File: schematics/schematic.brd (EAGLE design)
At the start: 180.3 x 63.5 mm, 22 parts, among them U1 TSR_1-2450

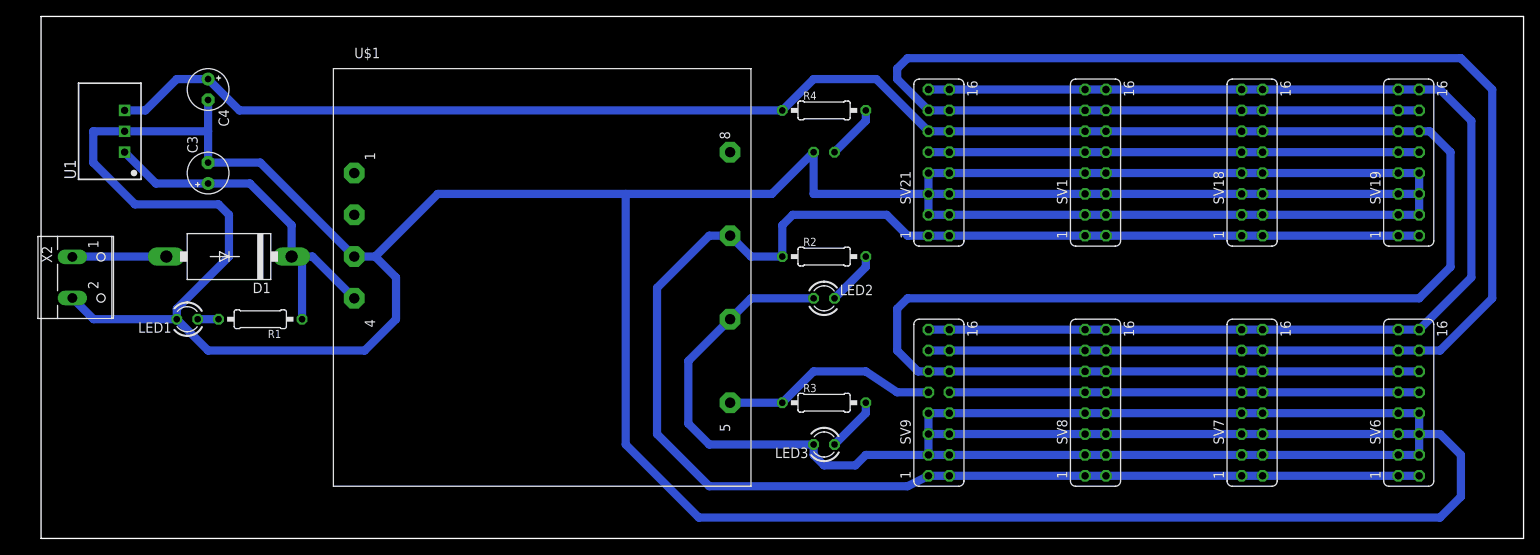
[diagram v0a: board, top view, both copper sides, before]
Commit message: added drillholes and descriptions
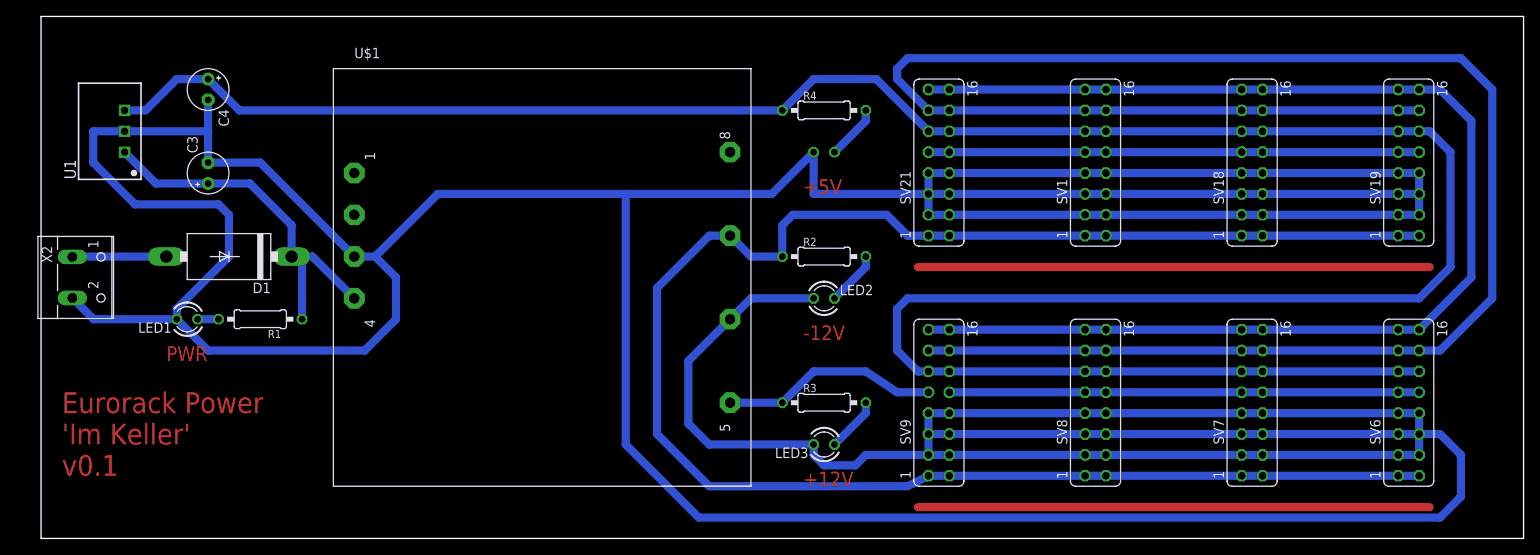
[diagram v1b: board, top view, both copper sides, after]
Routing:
- net N$6: track 0.00 -> 62.2 mm
- net N$1: track 0.00 -> 62.2 mm
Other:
- board text added: "+12V"
- board text added: "+5V"
- board text added: "-12V"
- board text added: "Eurorack Power 'Im Keller' v0.1"
- board text added: "PWR"
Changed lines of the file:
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@@
 <layer number="23" name="tOrigins" color="15" fill="1" visible="yes" active="yes"/>
 <layer number="24" name="bOrigins" color="15" fill="1" visible="yes" active="yes"/>
-<layer number="25" name="tNames" color="7" fill="1" visible="yes" active="yes"/>
+<layer number="25" name="tNames" color="16" fill="1" visible="yes" active="yes"/>
 <layer number="26" name="bNames" color="7" fill="1" visible="yes" active="yes"/>
 <layer number="27" name="tValues" color="7" fill="1" visible="yes" active="yes"/>
@@
 <wire x1="0" y1="0" x2="0" y2="63.5" width="0" layer="20"/>
 <dimension x1="0" y1="0" x2="0" y2="25.4" x3="-6.35" y3="12.7" textsize="1.778" layer="16"/>
+<text x="2.54" y="7.62" size="2.54" layer="1" font="fixed">Eurorack Power
+'Im Keller'
+v0.1</text>
+<text x="92.71" y="41.91" size="1.778" layer="1">+5V</text>
+<text x="92.71" y="24.13" size="1.778" layer="1">-12V</text>
+<text x="92.71" y="6.35" size="1.778" layer="1">+12V</text>
+<text x="15.24" y="21.59" size="1.778" layer="1">PWR</text>
+<circle x="3.81" y="3.81" radius="1.27" width="1" layer="44"/>
+<circle x="3.81" y="59.69" radius="1.27" width="1" layer="44"/>
+<circle x="176.53" y="3.81" radius="1.27" width="1" layer="44"/>
+<circle x="176.53" y="59.69" radius="1.27" width="1" layer="44"/>
 </plain>
 <attributes>
@@
 <wire x1="127" y1="20.32" x2="129.54" y2="20.32" width="0" layer="19" extent="1-1"/>
 </signal>
+<signal name="N$1">
+<wire x1="106.68" y1="3.81" x2="168.91" y2="3.81" width="1" layer="1"/>
+</signal>
+<signal name="N$6">
+<wire x1="106.68" y1="33.02" x2="168.91" y2="33.02" width="1" layer="1"/>
+</signal>
 </signals>
 <mfgpreviewcolors>
@@
 </drawing>
 <compatibility>
+<note version="6.3" minversion="6.2.2" severity="warning">
+Since Version 6.2.2 text objects can contain more than one line,
+which will not be processed correctly with this version.
+</note>
 <note version="8.2" severity="warning">
 Since Version 8.2, EAGLE supports online libraries. The ids

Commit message: added double input screw terminals
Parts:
- removed X2: (no value), con-wago-500:W237-102
- added X1: (no value), con-wago-500:W237-4
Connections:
- net +15V: now also X1.1, X1.2; no longer X2.1
- net GND: now also X1.3, X1.4; no longer X2.2
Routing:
- net +15V: track 11.4 -> 16.4 mm
- net GND: track 799.9 -> 803.5 mm
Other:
- board text added: "+"
- board text added: "-"
- board text added: "Eurorack Power 'Im Keller' v0.1 In: DC 9-18V 30W"
- board text removed: "Eurorack Power 'Im Keller' v0.1"
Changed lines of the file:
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@@
 <wire x1="0" y1="0" x2="0" y2="63.5" width="0" layer="20"/>
 <dimension x1="0" y1="0" x2="0" y2="25.4" x3="-6.35" y3="12.7" textsize="1.778" layer="16"/>
-<text x="2.54" y="7.62" size="2.54" layer="1" font="fixed">Eurorack Power
-'Im Keller'
-v0.1</text>
+<text x="2.54" y="7.62" size="2.1844" layer="1" font="fixed">Eurorack Power
+'Im Keller' v0.1
+In: DC 9-18V 30W</text>
 <text x="92.71" y="41.91" size="1.778" layer="1">+5V</text>
 <text x="92.71" y="24.13" size="1.778" layer="1">-12V</text>
@@
 <circle x="176.53" y="3.81" radius="1.27" width="1" layer="44"/>
 <circle x="176.53" y="59.69" radius="1.27" width="1" layer="44"/>
+<text x="11.43" y="39.37" size="2.54" layer="1" align="center">+</text>
+<text x="11.43" y="34.29" size="2.54" layer="1" align="center">+</text>
+<text x="11.43" y="29.21" size="2.54" layer="1" align="center">-</text>
+<text x="11.43" y="24.13" size="2.54" layer="1" align="center">-</text>
 </plain>
 <attributes>
@@
 <attribute name="VALUE" x="13.843" y="43.688" size="1.4224" layer="27" rot="R90"/>
 </element>
-<element name="X2" library="con-wago-500" library_urn="urn:adsk.eagle:library:195" package="W237-102" package3d_urn="urn:adsk.eagle:package:10688/1" value="" x="5.08" y="31.75" smashed="yes" rot="R270">
-<attribute name="MF" value="" x="-102.87" y="-64.77" size="1.778" layer="27" rot="R270" display="off"/>
-<attribute name="MPN" value="237-102" x="-102.87" y="-64.77" size="1.778" layer="27" rot="R270" display="off"/>
-<attribute name="NAME" x="0.0762" y="35.5962" size="1.27" layer="25" ratio="10" rot="R270"/>
-<attribute name="OC_FARNELL" value="unknown" x="-102.87" y="-64.77" size="1.778" layer="27" rot="R270" display="off"/>
-<attribute name="OC_NEWARK" value="70K9898" x="-102.87" y="-64.77" size="1.778" layer="27" rot="R270" display="off"/>
-<attribute name="POPULARITY" value="32" x="-102.87" y="-64.77" size="1.778" layer="27" rot="R270" display="off"/>
-<attribute name="VALUE" x="-2.54" y="36.79" size="1.27" layer="27" ratio="10" rot="R270"/>
-</element>
 <element name="C3" library="rcl" library_urn="urn:adsk.eagle:library:334" package="E2,5-5" package3d_urn="urn:adsk.eagle:package:23344/1" value="22uF" x="20.32" y="44.45" smashed="yes" rot="R90">
 <attribute name="NAME" x="19.05" y="46.863" size="1.27" layer="25" ratio="10" rot="R90"/>
@@
 <attribute name="VALUE" x="113.919" y="6.35" size="1.27" layer="27" ratio="10" rot="R90"/>
 </element>
+<element name="X1" library="con-wago-500" library_urn="urn:adsk.eagle:library:195" package="W237-4" package3d_urn="urn:adsk.eagle:package:10695/1" value="" x="5.08" y="31.75" smashed="yes" rot="R270">
+<attribute name="MF" value="" x="5.08" y="31.75" size="1.778" layer="27" rot="R270" display="off"/>
+<attribute name="MPN" value="" x="5.08" y="31.75" size="1.778" layer="27" rot="R270" display="off"/>
+<attribute name="NAME" x="-2.3622" y="40.4946" size="1.27" layer="25" ratio="10" rot="R270"/>
+<attribute name="OC_FARNELL" value="unknown" x="5.08" y="31.75" size="1.778" layer="27" rot="R270" display="off"/>
+<attribute name="OC_NEWARK" value="unknown" x="5.08" y="31.75" size="1.778" layer="27" rot="R270" display="off"/>
+<attribute name="POPULARITY" value="10" x="5.08" y="31.75" size="1.778" layer="27" rot="R270" display="off"/>
+<attribute name="VALUE" x="0.0508" y="39.4024" size="1.27" layer="27" ratio="10" rot="R270"/>
+</element>
 </elements>
 <signals>
 <signal name="GND">
-<contactref element="X2" pad="2"/>
 <contactref element="U$1" pad="3"/>
 <contactref element="U1" pad="2"/>
@@
 <contactref element="SV9" pad="3"/>
 <contactref element="SV9" pad="4"/>
-<wire x1="3.81" y1="29.25" x2="6.39" y2="26.67" width="1" layer="16"/>
-<wire x1="6.39" y1="26.67" x2="16.51" y2="26.67" width="1" layer="16"/>
 <wire x1="20.32" y1="45.72" x2="20.32" y2="49.53" width="1" layer="16"/>
 <wire x1="20.32" y1="49.53" x2="20.32" y2="53.34" width="1" layer="16"/>
@@
 <wire x1="80.01" y1="2.54" x2="71.12" y2="11.43" width="1" layer="16"/>
 <wire x1="71.12" y1="11.43" x2="71.12" y2="41.91" width="1" layer="16"/>
+<contactref element="X1" pad="3"/>
+<contactref element="X1" pad="4"/>
+<wire x1="16.51" y1="26.67" x2="6.39" y2="26.67" width="1" layer="16"/>
+<wire x1="3.81" y1="29.25" x2="6.39" y2="26.67" width="1" layer="16"/>
+<wire x1="6.39" y1="26.67" x2="3.97" y2="24.25" width="1" layer="16"/>
+<wire x1="3.97" y1="24.25" x2="3.81" y2="24.25" width="1" layer="16"/>
 <wire x1="165.1" y1="41.91" x2="165.1" y2="44.45" width="0" layer="19" extent="1-1"/>
 <wire x1="165.1" y1="39.37" x2="165.1" y2="41.91" width="0" layer="19" extent="1-1"/>
@@
 </signal>
 <signal name="+15V">
-<contactref element="X2" pad="1"/>
 <contactref element="D1" pad="A"/>
-<wire x1="3.81" y1="34.25" x2="3.85" y2="34.29" width="1" layer="16"/>
-<wire x1="3.85" y1="34.29" x2="15.24" y2="34.29" width="1" layer="16"/>
+<contactref element="X1" pad="2"/>
+<contactref element="X1" pad="1"/>
+<wire x1="15.24" y1="34.29" x2="15.2" y2="34.25" width="1" layer="16"/>
+<wire x1="15.2" y1="34.25" x2="3.81" y2="34.25" width="1" layer="16"/>
+<wire x1="3.81" y1="34.25" x2="3.81" y2="39.25" width="1" layer="16"/>
 </signal>
 <signal name="VI">

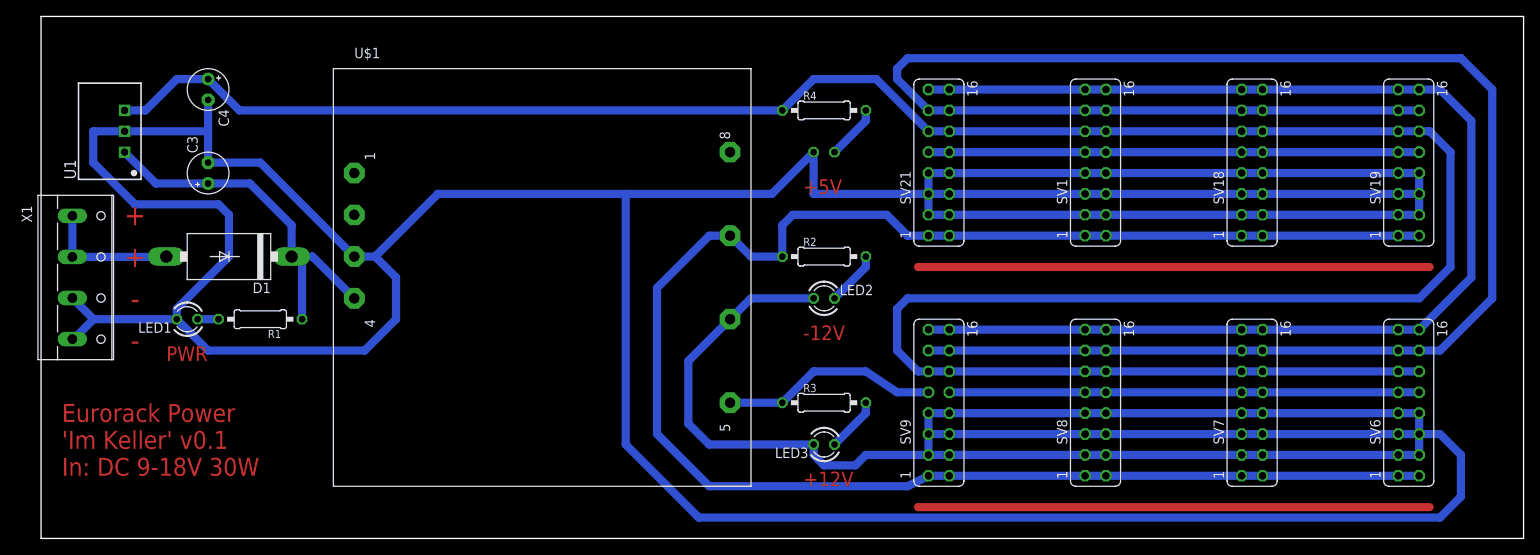
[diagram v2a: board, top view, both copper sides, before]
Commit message: removed airwire errors
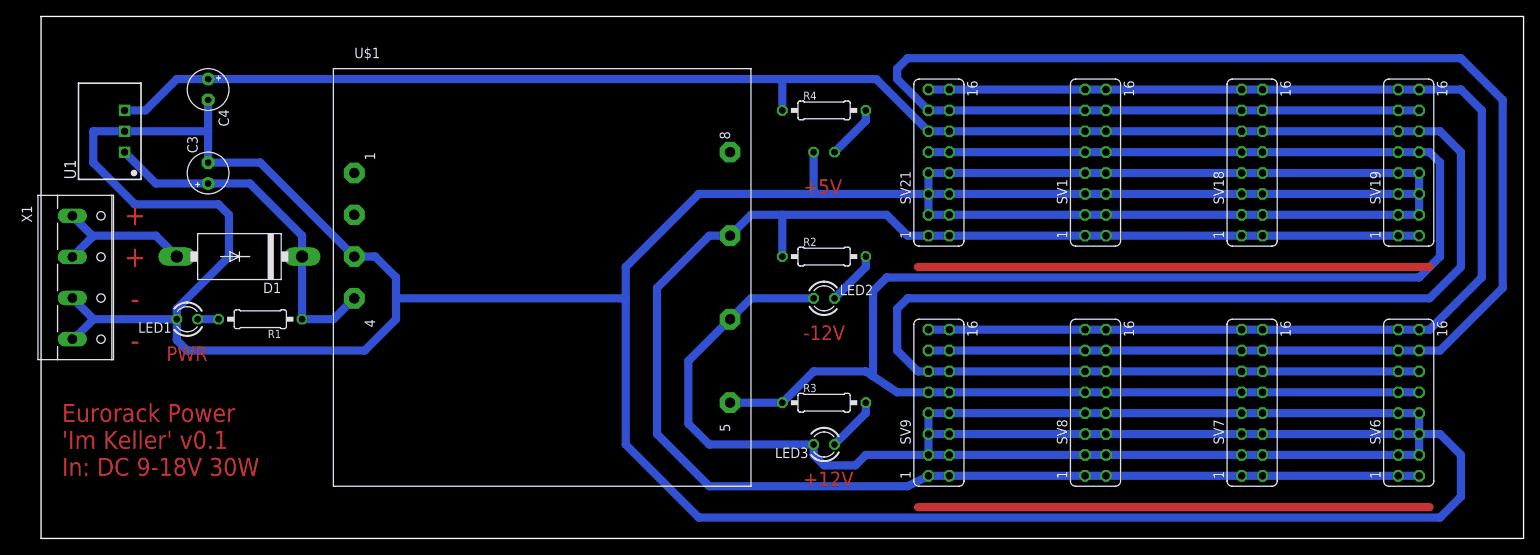
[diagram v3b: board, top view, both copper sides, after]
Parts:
- moved D1 1.27 mm to (24.1, 34.3)
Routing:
- net +12V: track 143.3 -> 241.4 mm
- net GND: track 803.5 -> 792.0 mm
- net GATE: track 155.3 -> 158.6 mm
- net +5V: track 322.7 -> 325.9 mm
- net +15V: track 16.4 -> 18.4 mm
- net VI: track 45.2 -> 43.4 mm
- net CV: track 237.5 -> 238.5 mm
- net -12V: track 215.2 -> 215.9 mm
